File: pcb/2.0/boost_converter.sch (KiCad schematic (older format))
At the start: 11 parts

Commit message: add the missing inductor footprint
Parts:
- L1: footprint components:Inductor_PIS2408_SMD -> kamaji:Inductor_PIS2408_SMD
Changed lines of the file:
@@
 F 0 "L1" V 5430 2990 50  0000 C CNN
 F 1 "10uH" V 5555 2990 50  0000 C CNN
-F 2 "components:Inductor_PIS2408_SMD" H 5480 2990 50  0001 C CNN
+F 2 "kamaji:Inductor_PIS2408_SMD" H 5480 2990 50  0001 C CNN
 F 3 "" H 5480 2990 50  0001 C CNN
 	1    5480 2990

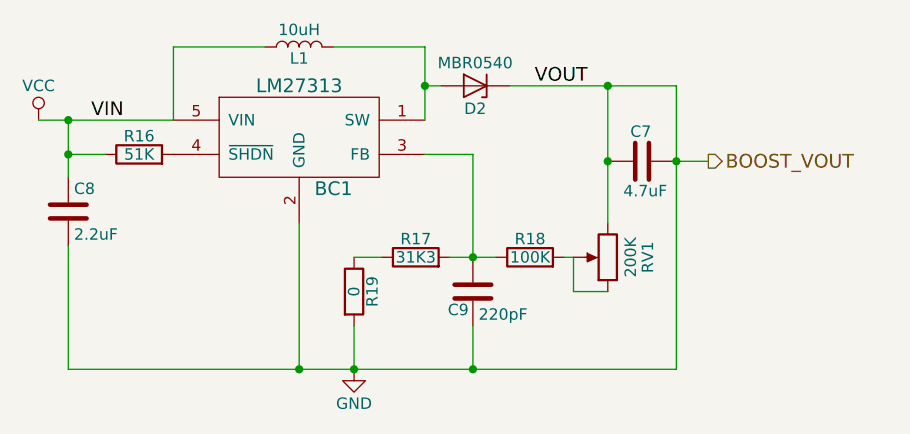
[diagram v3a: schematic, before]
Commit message: roughly place components on the PCB
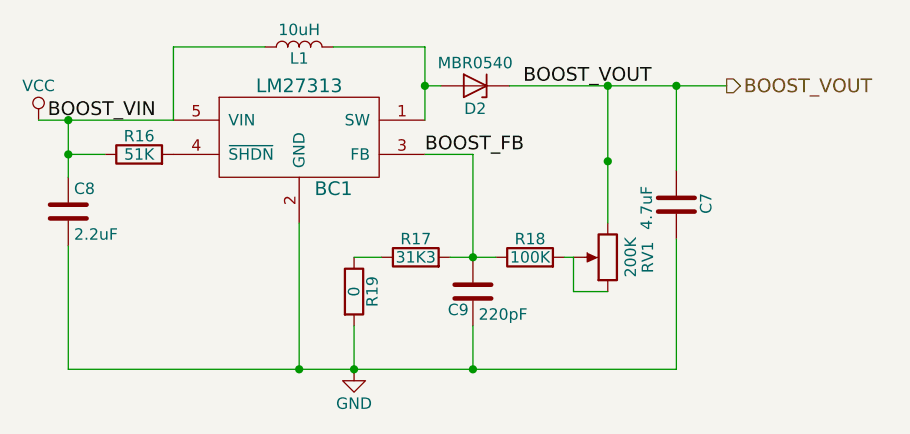
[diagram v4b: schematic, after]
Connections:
- net GND: no longer C7.1, D2.1 (K), RV1.3
- net BOOST_FB: now reaches BC1.3 (FB), C9.1, R17.2, R18.1
- new net BOOST_VOUT: C7.1, D2.1 (K), RV1.3
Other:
- moved on the sheet: C7
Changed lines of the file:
@@
 	1    0    0    -1
 $EndComp
-Text Label 4570 3310 0    60   ~ 0
-VIN
-Text Label 6510 3160 0    60   ~ 0
-VOUT
 $Comp
 L POT RV1
@@
 L C C7
 U 1 1 5A30CDFC
-P 6980 3490
-F 0 "C7" V 7110 3450 50  0000 L CNN
-F 1 "4.7uF" V 6850 3380 50  0000 L CNN
-F 2 "Capacitors_SMD:C_1206_HandSoldering" H 7018 3340 50  0001 C CNN
-F 3 "" H 6980 3490 50  0001 C CNN
-	1    6980 3490
-	0    -1   -1   0
+P 7130 3680
+F 0 "C7" V 7260 3640 50  0000 L CNN
+F 1 "4.7uF" V 7000 3570 50  0000 L CNN
+F 2 "Capacitors_SMD:C_1206_HandSoldering" H 7168 3530 50  0001 C CNN
+F 3 "" H 7130 3680 50  0001 C CNN
+	1    7130 3680
+	1    0    0    -1
 $EndComp
 $Comp
@@
 	1    0    0    -1
 $EndComp
-Text HLabel 7270 3490 2    60   Output ~ 0
+Text HLabel 7350 3160 2    60   Output ~ 0
 BOOST_VOUT
+$Comp
+L VCC #PWR053
+U 1 1 5A30F671
+P 4340 3310
+F 0 "#PWR053" H 4340 3160 50  0001 C CNN
+F 1 "VCC" H 4340 3460 50  0000 C CNN
+F 2 "" H 4340 3310 50  0001 C CNN
+F 3 "" H 4340 3310 50  0001 C CNN
+	1    4340 3310
+	1    0    0    -1
+$EndComp
+$Comp
+L GND #PWR054
+U 1 1 5A30FE4F
+P 5720 4400
+F 0 "#PWR054" H 5720 4150 50  0001 C CNN
+F 1 "GND" H 5720 4250 50  0000 C CNN
+F 2 "" H 5720 4400 50  0001 C CNN
+F 3 "" H 5720 4400 50  0001 C CNN
+	1    5720 4400
+	1    0    0    -1
+$EndComp
+Text Label 4380 3310 0    60   ~ 0
+BOOST_VIN
+Text Label 6460 3160 0    60   ~ 0
+BOOST_VOUT
+Text Label 6030 3460 0    60   ~ 0
+BOOST_FB
 Wire Wire Line
 	5630 2990 6030 2990
@@
 	4630 3460 4470 3460
 Wire Wire Line
-	6400 3160 7130 3160
-Wire Wire Line
 	6640 3910 6680 3910
 Wire Wire Line
@@
 Wire Wire Line
 	6830 3160 6830 3760
-Connection ~ 6830 3160
 Connection ~ 6830 3490
 Wire Wire Line
-	7130 3160 7130 4400
-Connection ~ 7130 3490
-Wire Wire Line
-	7270 3490 7130 3490
-$Comp
-L VCC #PWR059
-U 1 1 5A30F671
-P 4340 3310
-F 0 "#PWR059" H 4340 3160 50  0001 C CNN
-F 1 "VCC" H 4340 3460 50  0000 C CNN
-F 2 "" H 4340 3310 50  0001 C CNN
-F 3 "" H 4340 3310 50  0001 C CNN
-	1    4340 3310
-	1    0    0    -1
-$EndComp
-Wire Wire Line
-	7130 4400 4470 4400
+	4470 4400 7130 4400
 Connection ~ 5480 4400
 Connection ~ 5720 4400
 Connection ~ 6240 4400
-$Comp
-L GND #PWR060
-U 1 1 5A30FE4F
-P 5720 4400
-F 0 "#PWR060" H 5720 4150 50  0001 C CNN
-F 1 "GND" H 5720 4250 50  0000 C CNN
-F 2 "" H 5720 4400 50  0001 C CNN
-F 3 "" H 5720 4400 50  0001 C CNN
-	1    5720 4400
-	1    0    0    -1
-$EndComp
+Wire Wire Line
+	7130 4400 7130 3830
+Wire Wire Line
+	6400 3160 7350 3160
+Wire Wire Line
+	7130 3160 7130 3530
+Connection ~ 7130 3160
+Connection ~ 6830 3160
 $EndSCHEMATC

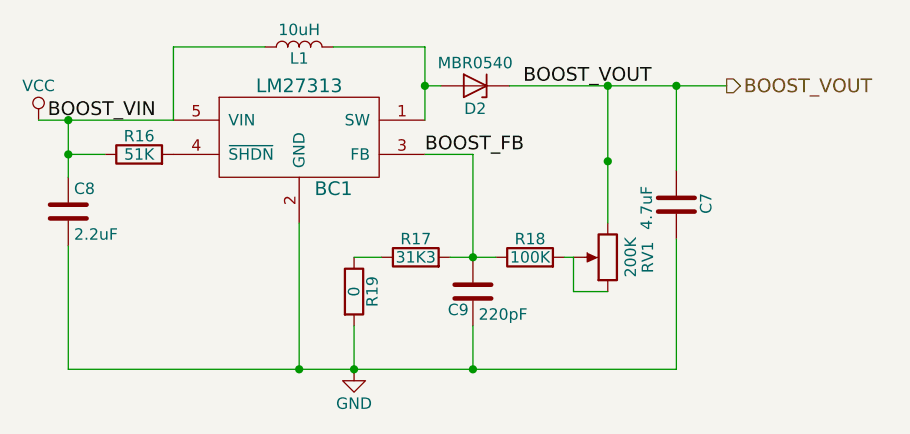
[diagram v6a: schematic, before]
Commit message: fix a resistor value
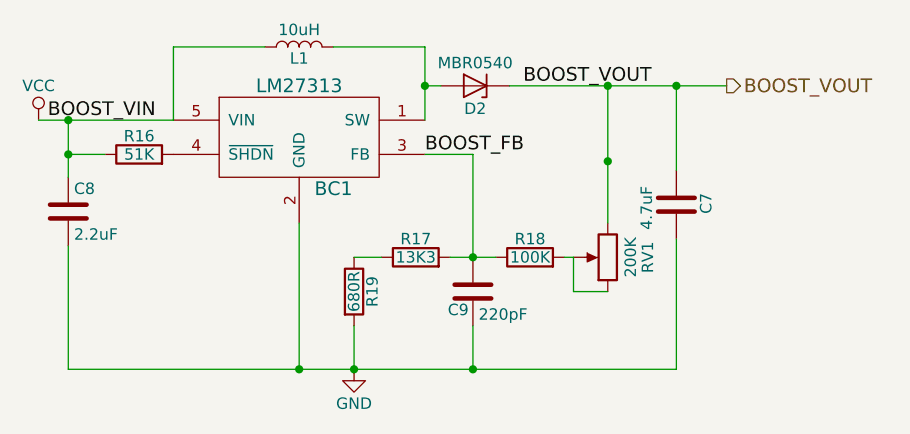
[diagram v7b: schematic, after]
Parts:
- R17: value 31K3 -> 13K3
- R19: value 0 -> 680R
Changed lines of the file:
@@
 P 5990 3910
 F 0 "R17" V 6070 3910 50  0000 C CNN
-F 1 "31K3" V 5990 3910 50  0000 C CNN
+F 1 "13K3" V 5990 3910 50  0000 C CNN
 F 2 "Resistors_SMD:R_1206_HandSoldering" V 5920 3910 50  0001 C CNN
 F 3 "" H 5990 3910 50  0001 C CNN
@@
 P 5720 4060
 F 0 "R19" V 5800 4060 50  0000 C CNN
-F 1 "0" V 5720 4060 50  0000 C CNN
+F 1 "680R" V 5720 4060 50  0000 C CNN
 F 2 "Resistors_SMD:R_1206_HandSoldering" V 5650 4060 50  0001 C CNN
 F 3 "" H 5720 4060 50  0001 C CNN
